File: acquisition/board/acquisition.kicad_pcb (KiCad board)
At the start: 6 copper layers, 103 x 90.5 mm, 432 parts, among them J1 XILINX_JTAG, J10 MMCX, J11 MMCX, J12 MMCX, J13 MMCX, J14 MMCX, J15 MMCX, J16 MMCX, J17 MMCX, J18 UX60SX-MB-5ST, J19 CONN_01X05, J2 MMCX, J20 CONN_01X06, J3 MMCX, J4 MMCX, J5 MMCX, J6 MMCX, J7 MMCX, J8 MMCX, J9 MMCX, Q1 SSM6N58NU, Q2 SSM6N58NU, U1 AD9251, U10 FT232HL, U11 LMK04806, U12 AK5DAF1-100.0000T2, U14 74AVCH1T45, U15 74AVCH1T45, U16 74AVCH1T45, U17 74AVCH1T45, U18 74AVCH1T45, U19 74AVCH1T45, U2 XC7A50T-1FTG256C, U20 74AVCH1T45, U21 ECS-3225MVQ-120-CN-TR, U22 93LC56B-MS, U23 74AVCH1T45, U24 74AVCH1T45, U25 LTC3374-QFN, U26 LT3042, U27 LT3042, U28 ADR510, U29 SIP32408, U3 AD9251, U30 LDO1117-12, U4 AD9251, U5 AD9251, U6 ICE40UP5K_QFN48, U7 STM32L031-QFN32, U8 S27KS0642, U9 S25FL128SAGBHIA10

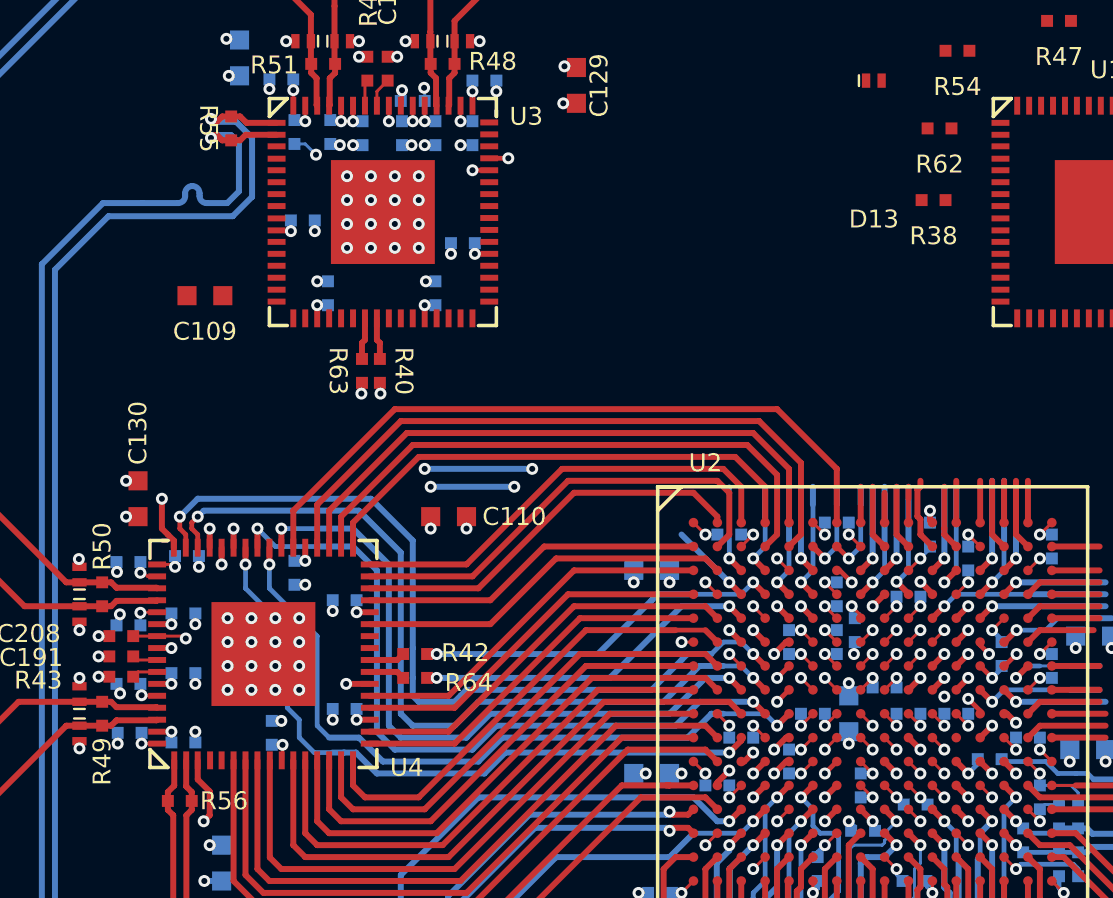
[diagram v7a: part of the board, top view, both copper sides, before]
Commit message: Routed most of third ADC data bus
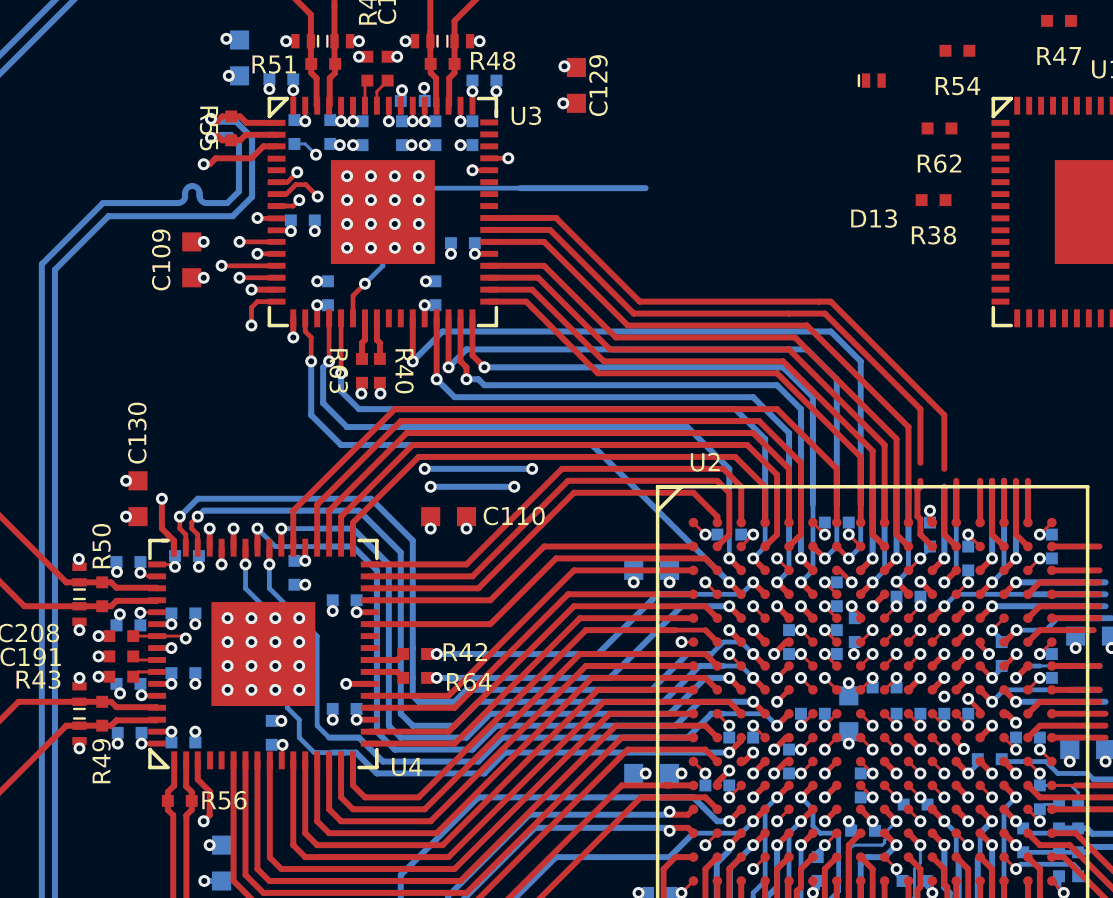
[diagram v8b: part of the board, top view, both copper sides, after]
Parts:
- moved C109 1.60 mm to (56.0, 49.0), turned to 90 degrees
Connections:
- U2 pad A10: /ADCs/D0_6 -> /ADCs/D2_9
- U2 pad A14: /ADCs/D2_0 -> /ADCs/ADC1_OE_N
- U2 pad A15: /ADCs/D2_4 -> /ADCs/D0_12
- U2 pad A8: /ADCs/D0_3 -> /ADCs/D2_5
- U2 pad A9: /ADCs/D0_4 -> /ADCs/D2_7
- U2 pad B10: /ADCs/D0_7 -> /ADCs/D2_8
- U2 pad B14: /ADCs/D2_2 -> /ADCs/D5_1
- U2 pad B15: /ADCs/D2_3 -> /ADCs/ADC0_CS_N
- U2 pad B6: /ADCs/D5_1 -> /ADCs/D2_2
- U2 pad B7: /ADCs/D5_11 -> /ADCs/D2_0
- U2 pad B9: /ADCs/D0_5 -> /ADCs/D2_6
- U2 pad C13: /ADCs/D5_4 -> /ADCs/ADC1_CS_N
- U2 pad C14: /ADCs/D2_1 -> /ADCs/D5_0
- U2 pad C16: /ADCs/D2_5 -> /ADCs/D0_3
- U2 pad C3: /ADCs/D5_3 -> /ADCs/D5_12
- U2 pad C4: /ADCs/ADC1_OE_N -> /ADCs/D5_13
- U2 pad C6: /ADCs/D5_8 -> /ADCs/D2_3
- U2 pad C7: /ADCs/D5_7 -> /ADCs/D5_4
- U2 pad D11: /ADCs/D2_6 -> /ADCs/D0_5
- U2 pad D14: /ADCs/D2_7 -> /ADCs/D0_4
- U2 pad D15: /ADCs/D2_8 -> /ADCs/D0_7
- U2 pad D3: /ADCs/D5_13 -> /ADCs/D5_11
- U2 pad D5: /ADCs/D5_6 -> /ADCs/D2_1
- U2 pad D6: /ADCs/D5_5 -> /ADCs/D2_4
- U2 pad D9: /ADCs/D0_12 -> /ADCs/D5_3
- U2 pad E5: /ADCs/D5_0 -> /ADCs/D5_6
- U2 pad E6: /ADCs/D5_12 -> /ADCs/D5_5
- U2 pad F12: /ADCs/D2_9 -> /ADCs/D0_6
- U2 pad F3: /ADCs/ADC0_CS_N -> /ADCs/D5_8
- U2 pad F4: /ADCs/ADC1_CS_N -> /ADCs/D5_7
- U2 pad G5: /ADCs/D5_9 -> /ADCs/D5_10
- U2 pad M12: /ADCs/D5_10 -> /ADCs/D5_9
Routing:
- net /ADCs/D5_3: track 3.71 -> 41.1 mm, vias 1 -> 2
- net /ADCs/D5_4: track 3.96 -> 38.9 mm, vias 1 -> 2
- net /ADCs/D5_6: track 4.91 -> 37.6 mm, vias 1 -> 2
- net /ADCs/D5_5: track 4.91 -> 35.8 mm, vias 1 -> 2
- net /ADCs/D5_7: track 5.34 -> 35.9 mm, vias 1 -> 2
- net /ADCs/D5_8: track 3.71 -> 34.1 mm, vias 1 -> 2
- net /ADCs/ADCCLK_2: track 1.17 -> 31.5 mm
- net /ADCs/D2_0: track 1.75 -> 30.7 mm, vias 0 -> 2
- net /ADCs/D5_9: track 20.5 -> 48.7 mm, vias 1 -> 3
- net /ADCs/D2_11: track 2.00 -> 26.7 mm
- net /ADCs/D2_2: track 2.96 -> 27.5 mm, vias 0 -> 2
- net /ADCs/D5_13: track 3.54 -> 27.5 mm, vias 1 -> 2
- net /ADCs/D2_4: track 1.75 -> 25.2 mm, vias 0 -> 2
- net /ADCs/D2_10: track 7.56 -> 31.0 mm
- net /ADCs/D2_6: track 0.73 -> 23.1 mm, vias 1 -> 0
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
